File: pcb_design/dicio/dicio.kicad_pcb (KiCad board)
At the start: 2 copper layers, 93 x 93 mm, 78 parts, among them J1 Conn_02x10_Odd_Even, J2 Conn_01x06_Female, J3 USB_C_Receptacle, J4 Micro_SD_Card, J5 USB_C_Receptacle, J6 USB_C_Receptacle, J8 USB_C_Receptacle, Q1 Q_NMOS_GSD, SW1 SW_SPST, SW2 SW_SPST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

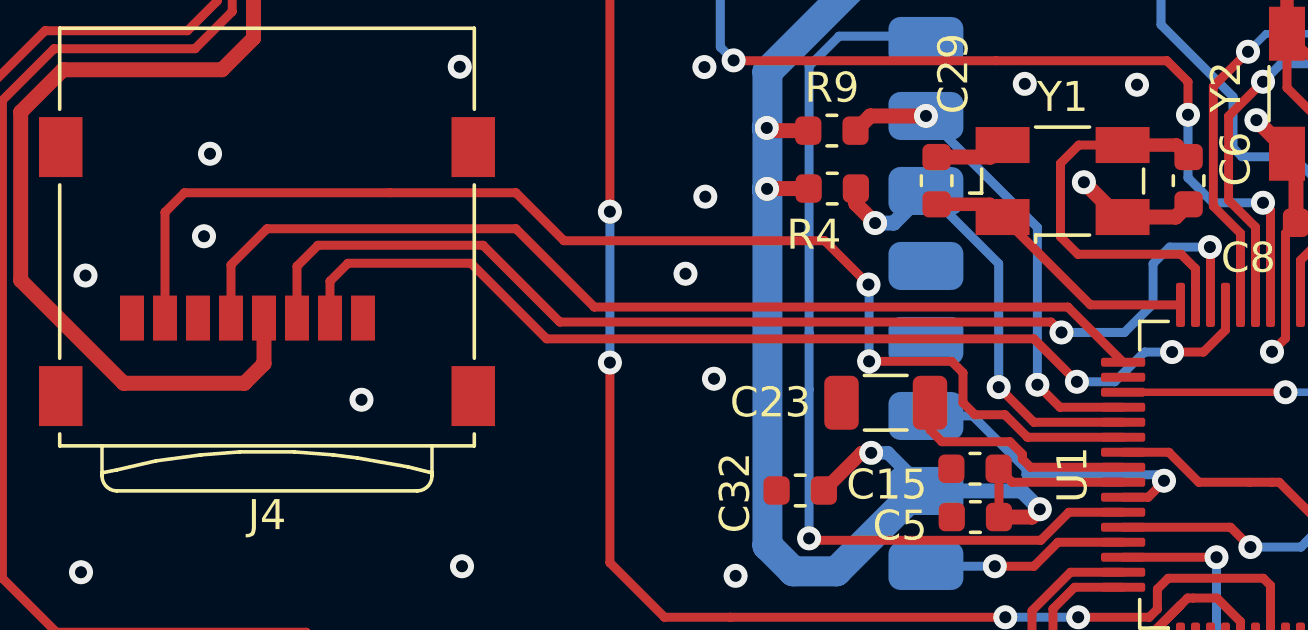
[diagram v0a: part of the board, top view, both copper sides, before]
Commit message: Change some component sizes
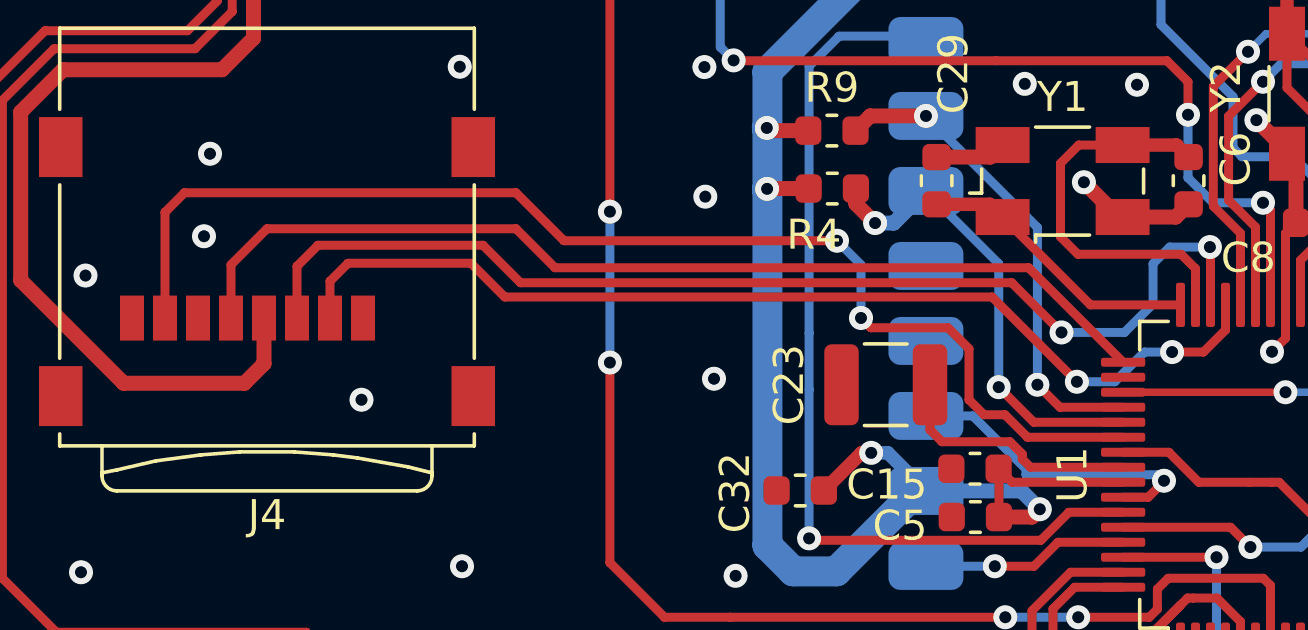
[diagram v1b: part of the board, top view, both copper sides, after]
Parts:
- C23: footprint Capacitor_SMD:C_1206_3216Metric -> Capacitor_SMD:C_1210_3225Metric
- moved C23 0.60 mm to (71.4, 82.0)
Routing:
- net GND: vias 92 -> 91

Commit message: Fix issue with labeling.
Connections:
- U1 pad 33: /USB_RX -> /USB_TX
- U1 pad 34: /USB_TX -> /USB_RX
- U8 pad 1: /USB_TX -> /USB_RX
- U8 pad 5: /USB_RX -> /USB_TX
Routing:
- net /USB_TX: track 40.1 -> 39.6 mm, vias 4 -> 0
- net /USB_RX: track 39.6 -> 40.1 mm, vias 0 -> 4

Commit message: Various updates for Aisler order.
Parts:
- C29, C6: value 20pF -> 22pF
- C7, C8: value 20pF -> 30pF
- Y1: value Crystal_GND24 -> Crystal; footprint Crystal:Crystal_SMD_Abracon_ABM3B-4Pin_5.0x3.2mm -> Crystal:Crystal_SMD_3215-2Pin_3.2x1.5mm
- moved C29 2.92 mm to (76.0, 75.7)
- moved C6 2.66 mm to (79.4, 73.6), turned to 0 degrees
- moved Y1 1.86 mm to (79.0, 76.0), turned to 180 degrees
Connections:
- Y1 pad 2: GND -> /SOSC1
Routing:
- net /SOSC1: track 13.3 -> 6.39 mm
- net GND: track 87.8 -> 81.3 mm, vias 91 -> 90
- net /SOSC2: track 9.52 -> 8.50 mm

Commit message: Updates
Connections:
- J3 pad A10: /SCL2 -> /SCL1
- J3 pad A2: /~{INT2} -> /~{INT1}
- J3 pad A3: /SDA2 -> /SDA1
- J3 pad B10: /SCL2 -> /SCL1
- J3 pad B2: /~{INT2} -> /~{INT1}
- J3 pad B3: /SDA2 -> /SDA1
- J5 pad A10: /SCL1 -> /SCL2
- J5 pad A2: /~{INT1} -> /~{INT2}
- J5 pad A3: /SDA1 -> /SDA2
- J5 pad A6: /OW2 -> /OW3
- J5 pad A7: /AS2 -> /AS3
- J5 pad B10: /SCL1 -> /SCL2
- J5 pad B2: /~{INT1} -> /~{INT2}
- J5 pad B3: /SDA1 -> /SDA2
- J5 pad B6: /OW2 -> /OW3
- J5 pad B7: /AS2 -> /AS3
- J6 pad A10: /SCL2 -> /SCL1
- J6 pad A2: /~{INT2} -> /~{INT1}
- J6 pad A3: /SDA2 -> /SDA1
- J6 pad A6: /OW3 -> /OW2
- J6 pad A7: /AS3 -> /AS2
- J6 pad B10: /SCL2 -> /SCL1
- J6 pad B2: /~{INT2} -> /~{INT1}
- J6 pad B3: /SDA2 -> /SDA1
- J6 pad B6: /OW3 -> /OW2
- J6 pad B7: /AS3 -> /AS2
- J8 pad A10: /SCL1 -> /SCL2
- J8 pad A2: /~{INT1} -> /~{INT2}
- J8 pad A3: /SDA1 -> /SDA2
- J8 pad B10: /SCL1 -> /SCL2
- J8 pad B2: /~{INT1} -> /~{INT2}
- J8 pad B3: /SDA1 -> /SDA2
- R12 pad 2: /SDA2 -> /SDA1
- R13 pad 2: /SCL2 -> /SCL1
- R14 pad 2: /SDA1 -> /SDA2
- R15 pad 2: /SCL1 -> /SCL2
- R22 pad 2: /~{INT1} -> /~{INT2}
- R24 pad 2: /~{INT2} -> /~{INT1}
- U1 pad 12: /~{INT1} -> /~{INT2}
- U1 pad 13: /OW2 -> /OW3
- U1 pad 14: /AS2 -> /AS3
- U1 pad 3: /OW3 -> /OW2
- U1 pad 31: /SDA1 -> /SDA2
- U1 pad 32: /SCL1 -> /SCL2
- U1 pad 43: /SDA2 -> /SDA1
- U1 pad 44: /SCL2 -> /SCL1
- U1 pad 62: /~{INT2} -> /~{INT1}
- U1 pad 63: /AS3 -> /AS2
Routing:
- net /SCL2: track 169.3 -> 113.7 mm, vias 13 -> 11
- net /SCL1: track 113.7 -> 169.3 mm, vias 11 -> 13
- net /SDA2: track 162.9 -> 124.2 mm, vias 10 -> 13
- net /SDA1: track 124.2 -> 162.9 mm, vias 13 -> 10
- net /~{INT2}: track 97.4 -> 116.7 mm, vias 8 -> 4
- net /~{INT1}: track 116.7 -> 97.4 mm, vias 4 -> 8
- net /OW3: track 48.2 -> 43.1 mm
- net /OW2: track 43.1 -> 48.2 mm
- net /AS3: track 42.8 -> 39.6 mm, vias 2 -> 0
- net /AS2: track 39.6 -> 42.8 mm, vias 0 -> 2
